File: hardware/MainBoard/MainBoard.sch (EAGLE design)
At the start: 220 parts, among them J1 CON-71741-2184-BOT, J2 CON-71741-2184-TOP, J3 CON-FTSH-105-01-L-DV-K, J4 CON-ZX62R-B-5P, J5 CON-SMA, J6 CON-SMA, J7 CON-RJ45-J0G-0007NL, J8 SWITCH-CJS-1200-1200, M1 MOUNT-HOLE3.3, M2 MOUNT-HOLE3.3, M3 MOUNT-HOLE3.3, M4 MOUNT-HOLE3.3, M5 FIDUCIAL1X2, M6 FIDUCIAL1X2, M7 FIDUCIAL1X2, M8 FIDUCIAL1X2, Q1 MMBT3904, SW1 SWITCH-KSC-201J, SW2 SWITCH-KSC-201J, U1 A2F500M3G-FG256, U2 MAX19706-T4877-4, U3 MAX19706-T4877-4, U4 USBLC6-2SC6, U5 FT232HL, U6 DP83848C-VBH48A, U7 93LC56BT-OT, U8 DS1818-10-SOT-23, U9 LMV112, X1 FOX924B, X2 ECX-31B, X3 ASEM1-C, X5 ECX-42-120

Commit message: Routed external clocks (still needs adjustment).
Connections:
- net D3V3: no longer C74.1, C75.1, C76.1
- net VJTAG: now also C74.1
- net VPUMP: now also C75.1, C76.1
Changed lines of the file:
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@@
 <part name="C74" library="MainBoard" deviceset="C" device="0402" value="0.1uF"/>
 <part name="U$87" library="MainBoard" deviceset="DGND" device=""/>
-<part name="U$88" library="MainBoard" deviceset="D3V3" device=""/>
 <part name="C75" library="MainBoard" deviceset="C" device="0402" value="0.33uF">
 <attribute name="VOTLAGE-RATING" value="16V"/>
@@
 </part>
 <part name="U$91" library="MainBoard" deviceset="DGND" device=""/>
-<part name="U$92" library="MainBoard" deviceset="D3V3" device=""/>
 <part name="PORT198" library="MainBoard" deviceset="PORT5" device=""/>
 <part name="PORT209" library="MainBoard" deviceset="PORT5" device=""/>
@@
 <part name="PORT359" library="MainBoard" deviceset="PORT7" device=""/>
 <part name="PORT360" library="MainBoard" deviceset="PORT7" device=""/>
+<part name="PORT361" library="MainBoard" deviceset="PORT5" device=""/>
+<part name="PORT362" library="MainBoard" deviceset="PORT5" device=""/>
 </parts>
 <sheets>
@@
 <rectangle x1="50.8" y1="81.28" x2="60.96" y2="83.82" layer="101"/>
 <text x="39.37" y="87.63" size="1.778" layer="101">Check if it should be negated</text>
-<rectangle x1="22.86" y1="68.58" x2="101.6" y2="91.44" layer="116"/>
 <rectangle x1="137.16" y1="121.92" x2="228.6" y2="165.1" layer="116"/>
 <rectangle x1="172.72" y1="43.18" x2="195.58" y2="78.74" layer="116"/>
 <rectangle x1="205.74" y1="43.18" x2="215.9" y2="78.74" layer="116"/>
 <rectangle x1="132.08" y1="81.28" x2="231.14" y2="119.38" layer="116"/>
+<rectangle x1="25.4" y1="71.12" x2="63.5" y2="91.44" layer="116"/>
+<rectangle x1="63.5" y1="71.12" x2="104.14" y2="81.28" layer="116"/>
 </plain>
 <instances>
@@
 <instance part="C74" gate="G$1" x="200.66" y="55.88"/>
 <instance part="U$87" gate="G$1" x="200.66" y="43.18"/>
-<instance part="U$88" gate="G$1" x="200.66" y="63.5"/>
 <instance part="C75" gate="G$1" x="218.44" y="55.88">
 <attribute name="VOTLAGE-RATING" x="218.44" y="55.88" size="1.778" layer="96" display="off"/>
@@
 </instance>
 <instance part="U$91" gate="G$1" x="220.98" y="43.18"/>
-<instance part="U$92" gate="G$1" x="220.98" y="63.5"/>
 <instance part="PORT198" gate="G$1" x="175.26" y="73.66" rot="R90"/>
 <instance part="PORT209" gate="G$1" x="182.88" y="73.66" rot="R90"/>
@@
 <instance part="PORT317" gate="G$1" x="193.04" y="45.72" rot="R270"/>
 <instance part="U$20" gate="G$1" x="30.48" y="33.02"/>
+<instance part="PORT361" gate="G$1" x="200.66" y="73.66" rot="R90"/>
+<instance part="PORT362" gate="G$1" x="220.98" y="73.66" rot="R90"/>
 </instances>
 <busses>
@@
 <wire x1="220.98" y1="114.3" x2="220.98" y2="116.84" width="0.1524" layer="91"/>
 <pinref part="U$90" gate="G$1" pin="D3V3"/>
-</segment>
-<segment>
-<pinref part="C74" gate="G$1" pin="1"/>
-<wire x1="200.66" y1="58.42" x2="200.66" y2="63.5" width="0.1524" layer="91"/>
-<pinref part="U$88" gate="G$1" pin="D3V3"/>
-</segment>
-<segment>
-<pinref part="C75" gate="G$1" pin="1"/>
-<wire x1="218.44" y1="58.42" x2="218.44" y2="60.96" width="0.1524" layer="91"/>
-<pinref part="C76" gate="G$1" pin="1"/>
-<wire x1="223.52" y1="58.42" x2="223.52" y2="60.96" width="0.1524" layer="91"/>
-<wire x1="223.52" y1="60.96" x2="220.98" y2="60.96" width="0.1524" layer="91"/>
-<pinref part="U$92" gate="G$1" pin="D3V3"/>
-<wire x1="220.98" y1="60.96" x2="218.44" y2="60.96" width="0.1524" layer="91"/>
-<wire x1="220.98" y1="63.5" x2="220.98" y2="60.96" width="0.1524" layer="91"/>
-<junction x="220.98" y="60.96"/>
 </segment>
 <segment>
@@
 <label x="144.78" y="106.68" size="1.778" layer="95" rot="MR0"/>
 </segment>
+<segment>
+<pinref part="C74" gate="G$1" pin="1"/>
+<wire x1="200.66" y1="58.42" x2="200.66" y2="63.5" width="0.1524" layer="91"/>
+<label x="200.66" y="66.04" size="1.778" layer="95" rot="R90"/>
+</segment>
 </net>
 <net name="VPUMP" class="0">
@@
 <label x="200.66" y="106.68" size="1.778" layer="95"/>
 </segment>
-</net>
+<segment>
+<pinref part="C75" gate="G$1" pin="1"/>
+<wire x1="218.44" y1="58.42" x2="218.44" y2="60.96" width="0.1524" layer="91"/>
+<pinref part="C76" gate="G$1" pin="1"/>
+<wire x1="223.52" y1="58.42" x2="223.52" y2="60.96" width="0.1524" layer="91"/>
+<wire x1="223.52" y1="60.96" x2="220.98" y2="60.96" width="0.1524" layer="91"/>
+<wire x1="220.98" y1="60.96" x2="218.44" y2="60.96" width="0.1524" layer="91"/>
+<wire x1="220.98" y1="63.5" x2="220.98" y2="60.96" width="0.1524" layer="91"/>
+<junction x="220.98" y="60.96"/>
+<label x="220.98" y="66.04" size="1.778" layer="95" rot="R90"/>
+</segment>
+</net>

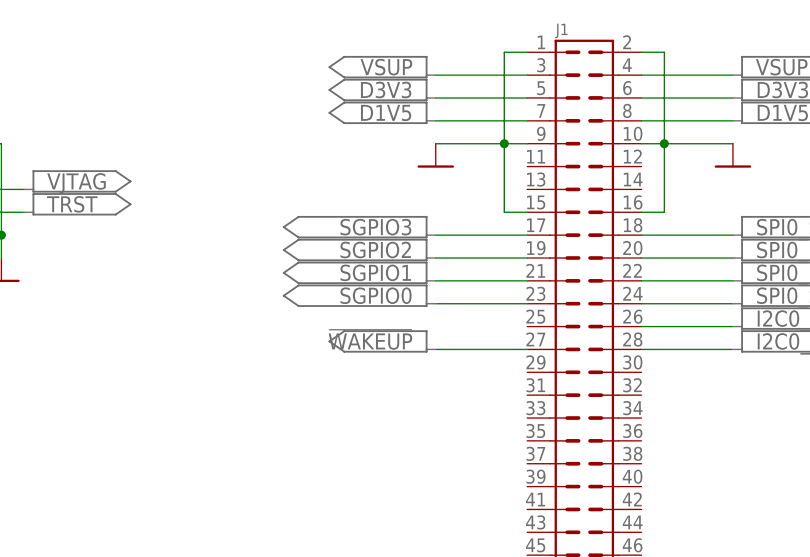
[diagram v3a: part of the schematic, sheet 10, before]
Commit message: 
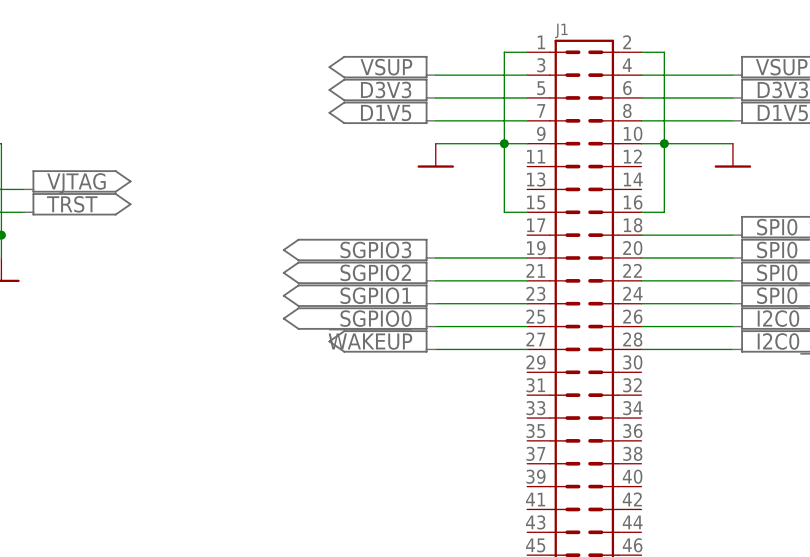
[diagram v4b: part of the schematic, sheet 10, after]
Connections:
- net NGPIO3: now also U1-EXTERNAL-MEMORY-CONTROLLER.EMC_CLK/GAA0/IO02NDB0V0; no longer U1-EXTERNAL-MEMORY-CONTROLLER.EMC_DB[6]/GEB0/IO79NDB5V0
- net NGPIO4: now also U1-IOB.IO84NDB5V0; no longer U1-EXTERNAL-MEMORY-CONTROLLER.EMC_DB[7]/GEB1/IO79PDB5V0
- net SGPIO0: now also J1.25; no longer J1.23
- net SGPIO1: now also J1.23; no longer J1.21
- net SGPIO2: now also J1.21, U1-EXTERNAL-MEMORY-CONTROLLER.EMC_DB[6]/GEB0/IO79NDB5V0; no longer J1.19, U1-EXTERNAL-MEMORY-CONTROLLER.EMC_CLK/GAA0/IO02NDB0V0
- net SGPIO3: now also J1.19, U1-EXTERNAL-MEMORY-CONTROLLER.EMC_DB[7]/GEB1/IO79PDB5V0; no longer J1.17, U1-IOB.IO84NDB5V0

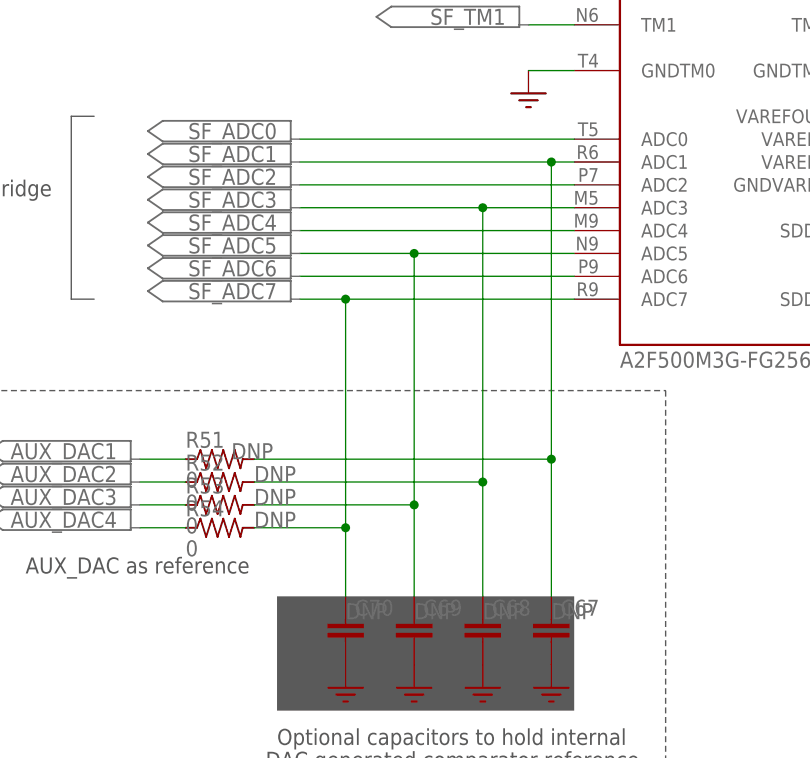
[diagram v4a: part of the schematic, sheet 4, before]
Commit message: 
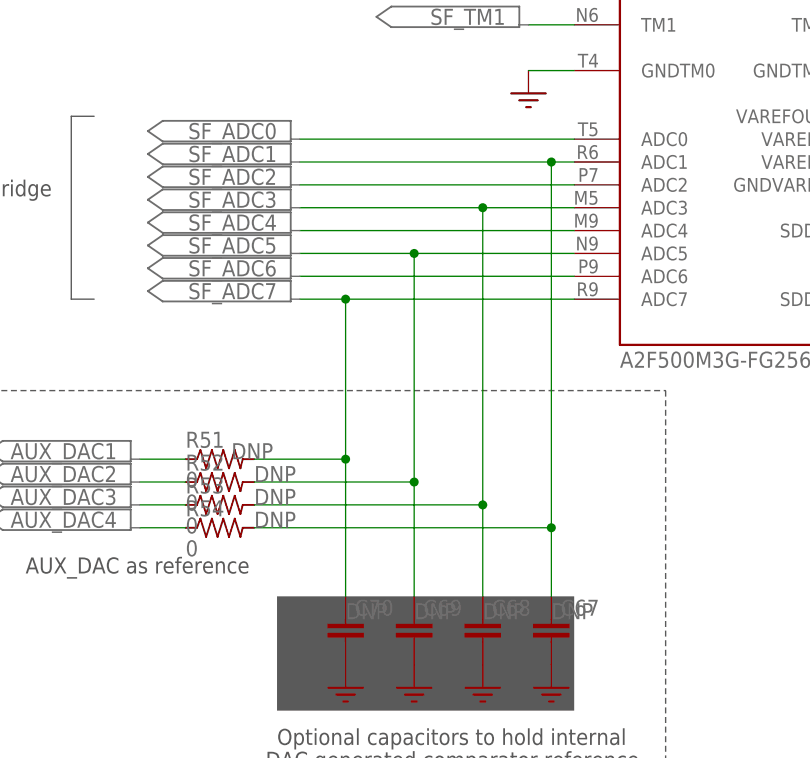
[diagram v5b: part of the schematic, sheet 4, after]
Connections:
- net NGPIO0: now also U1-EXTERNAL-MEMORY-CONTROLLER.EMC_DB[6]/GEB0/IO79NDB5V0; no longer U1-EXTERNAL-MEMORY-CONTROLLER.EMC_DB[2]/IO77NDB5V0
- net NGPIO1: now also U1-EXTERNAL-MEMORY-CONTROLLER.EMC_DB[10]/IO86NPB5V0; no longer U1-EXTERNAL-MEMORY-CONTROLLER.EMC_DB[5]/GEA1/IO78PPB5V0
- net NGPIO2: now also U1-EXTERNAL-MEMORY-CONTROLLER.EMC_DB[11]/IO86PPB5V0; no longer U1-EXTERNAL-MEMORY-CONTROLLER.EMC_DB[8]/GEC0/IO80NDB5V0
- net SF_ADC1: now also R54.2; no longer R51.2
- net SF_ADC3: now also R53.2; no longer R52.2
- net SF_ADC5: now also R52.2; no longer R53.2
- net SF_ADC7: now also R51.2; no longer R54.2
- net SGPIO0: now also U1-EXTERNAL-MEMORY-CONTROLLER.EMC_DB[5]/GEA1/IO78PPB5V0; no longer U1-EXTERNAL-MEMORY-CONTROLLER.EMC_DB[10]/IO86NPB5V0
- net SGPIO1: now also U1-EXTERNAL-MEMORY-CONTROLLER.EMC_DB[8]/GEC0/IO80NDB5V0; no longer U1-EXTERNAL-MEMORY-CONTROLLER.EMC_DB[11]/IO86PPB5V0
- net SGPIO2: now also U1-EXTERNAL-MEMORY-CONTROLLER.EMC_DB[2]/IO77NDB5V0; no longer U1-EXTERNAL-MEMORY-CONTROLLER.EMC_DB[6]/GEB0/IO79NDB5V0
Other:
- note added: "Check assignment order (routing!)"
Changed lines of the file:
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@@
 <text x="205.74" y="60.96" size="1.778" layer="97" rot="R90">VAREF0</text>
 <text x="213.36" y="60.96" size="1.778" layer="97" rot="R90">VAREF1</text>
+<rectangle x1="73.66" y1="53.34" x2="106.68" y2="63.5" layer="98"/>
+<text x="71.12" y="50.8" size="1.778" layer="98">Check assignment order (routing!)</text>
+<rectangle x1="40.64" y1="50.8" x2="71.12" y2="68.58" layer="116"/>
+<rectangle x1="71.12" y1="35.56" x2="111.76" y2="50.8" layer="116"/>
+<rectangle x1="132.08" y1="63.5" x2="154.94" y2="83.82" layer="116"/>
+<rectangle x1="182.88" y1="38.1" x2="226.06" y2="73.66" layer="116"/>
+<rectangle x1="142.24" y1="99.06" x2="185.42" y2="119.38" layer="116"/>
 </plain>
 <instances>
@@
 <wire x1="101.6" y1="96.52" x2="73.66" y2="96.52" width="0.1524" layer="91"/>
 <junction x="101.6" y="96.52"/>
-<wire x1="101.6" y1="48.26" x2="101.6" y2="63.5" width="0.1524" layer="91"/>
-<pinref part="R51" gate="G$1" pin="2"/>
-<wire x1="101.6" y1="63.5" x2="101.6" y2="96.52" width="0.1524" layer="91"/>
-<wire x1="68.58" y1="63.5" x2="101.6" y2="63.5" width="0.1524" layer="91"/>
-<junction x="101.6" y="63.5"/>
+<wire x1="101.6" y1="48.26" x2="101.6" y2="55.88" width="0.1524" layer="91"/>
+<pinref part="R54" gate="G$1" pin="2"/>
+<wire x1="101.6" y1="55.88" x2="101.6" y2="96.52" width="0.1524" layer="91"/>
+<wire x1="68.58" y1="55.88" x2="101.6" y2="55.88" width="0.1524" layer="91"/>
+<junction x="101.6" y="55.88"/>
 </segment>
 </net>
@@
 <wire x1="93.98" y1="91.44" x2="73.66" y2="91.44" width="0.1524" layer="91"/>
 <junction x="93.98" y="91.44"/>
-<wire x1="93.98" y1="48.26" x2="93.98" y2="60.96" width="0.1524" layer="91"/>
-<pinref part="R52" gate="G$1" pin="2"/>
-<wire x1="93.98" y1="60.96" x2="93.98" y2="91.44" width="0.1524" layer="91"/>
-<wire x1="68.58" y1="60.96" x2="93.98" y2="60.96" width="0.1524" layer="91"/>
-<junction x="93.98" y="60.96"/>
+<wire x1="93.98" y1="48.26" x2="93.98" y2="58.42" width="0.1524" layer="91"/>
+<pinref part="R53" gate="G$1" pin="2"/>
+<wire x1="93.98" y1="58.42" x2="93.98" y2="91.44" width="0.1524" layer="91"/>
+<wire x1="68.58" y1="58.42" x2="93.98" y2="58.42" width="0.1524" layer="91"/>
+<junction x="93.98" y="58.42"/>
 </segment>
 </net>
@@
 <wire x1="86.36" y1="86.36" x2="73.66" y2="86.36" width="0.1524" layer="91"/>
 <junction x="86.36" y="86.36"/>
-<wire x1="86.36" y1="48.26" x2="86.36" y2="58.42" width="0.1524" layer="91"/>
-<pinref part="R53" gate="G$1" pin="2"/>
-<wire x1="86.36" y1="58.42" x2="86.36" y2="86.36" width="0.1524" layer="91"/>
-<wire x1="68.58" y1="58.42" x2="86.36" y2="58.42" width="0.1524" layer="91"/>
-<junction x="86.36" y="58.42"/>
+<wire x1="86.36" y1="48.26" x2="86.36" y2="60.96" width="0.1524" layer="91"/>
+<pinref part="R52" gate="G$1" pin="2"/>
+<wire x1="86.36" y1="60.96" x2="86.36" y2="86.36" width="0.1524" layer="91"/>
+<wire x1="68.58" y1="60.96" x2="86.36" y2="60.96" width="0.1524" layer="91"/>
+<junction x="86.36" y="60.96"/>
 </segment>
 </net>
@@
 <wire x1="78.74" y1="81.28" x2="73.66" y2="81.28" width="0.1524" layer="91"/>
 <junction x="78.74" y="81.28"/>
-<wire x1="78.74" y1="48.26" x2="78.74" y2="55.88" width="0.1524" layer="91"/>
-<pinref part="R54" gate="G$1" pin="2"/>
-<wire x1="78.74" y1="55.88" x2="78.74" y2="81.28" width="0.1524" layer="91"/>
-<wire x1="68.58" y1="55.88" x2="78.74" y2="55.88" width="0.1524" layer="91"/>
-<junction x="78.74" y="55.88"/>
+<wire x1="78.74" y1="48.26" x2="78.74" y2="63.5" width="0.1524" layer="91"/>
+<pinref part="R51" gate="G$1" pin="2"/>
+<wire x1="78.74" y1="63.5" x2="78.74" y2="81.28" width="0.1524" layer="91"/>
+<wire x1="68.58" y1="63.5" x2="78.74" y2="63.5" width="0.1524" layer="91"/>
+<junction x="78.74" y="63.5"/>
 </segment>
 </net>
@@
 </segment>
 </net>
-<net name="NGPIO0" class="0">
-<segment>
-<pinref part="U1" gate="-EXTERNAL-MEMORY-CONTROLLER" pin="EMC_DB[2]/IO77NDB5V0"/>
-<wire x1="215.9" y1="149.86" x2="220.98" y2="149.86" width="0.1524" layer="91"/>
-<label x="223.52" y="149.86" size="1.778" layer="95"/>
-</segment>
-</net>
 <net name="NGPIO1" class="0">
 <segment>
-<pinref part="U1" gate="-EXTERNAL-MEMORY-CONTROLLER" pin="EMC_DB[5]/GEA1/IO78PPB5V0"/>
-<wire x1="215.9" y1="142.24" x2="220.98" y2="142.24" width="0.1524" layer="91"/>
-<label x="223.52" y="142.24" size="1.778" layer="95"/>
-</segment>
-</net>
-<net name="SGPIO0" class="0">
-<segment>
 <pinref part="U1" gate="-EXTERNAL-MEMORY-CONTROLLER" pin="EMC_DB[10]/IO86NPB5V0"/>
 <wire x1="215.9" y1="129.54" x2="220.98" y2="129.54" width="0.1524" layer="91"/>
@@
 </segment>
 </net>
-<net name="SGPIO1" class="0">
+<net name="NGPIO2" class="0">
 <segment>
 <pinref part="U1" gate="-EXTERNAL-MEMORY-CONTROLLER" pin="EMC_DB[11]/IO86PPB5V0"/>
@@
 </segment>
 </net>
-<net name="NGPIO2" class="0">
-<segment>
-<pinref part="U1" gate="-EXTERNAL-MEMORY-CONTROLLER" pin="EMC_DB[8]/GEC0/IO80NDB5V0"/>
-<wire x1="215.9" y1="134.62" x2="220.98" y2="134.62" width="0.1524" layer="91"/>
-<label x="223.52" y="134.62" size="1.778" layer="95"/>
-</segment>
-</net>
 <net name="SGPIO3" class="0">
 <segment>
@@
 <net name="SGPIO2" class="0">
 <segment>
-<pinref part="U1" gate="-EXTERNAL-MEMORY-CONTROLLER" pin="EMC_DB[6]/GEB0/IO79NDB5V0"/>
-<wire x1="215.9" y1="139.7" x2="220.98" y2="139.7" width="0.1524" layer="91"/>
-<label x="223.52" y="139.7" size="1.778" layer="95"/>
+<pinref part="U1" gate="-EXTERNAL-MEMORY-CONTROLLER" pin="EMC_DB[2]/IO77NDB5V0"/>
+<wire x1="215.9" y1="149.86" x2="220.98" y2="149.86" width="0.1524" layer="91"/>
+<label x="223.52" y="149.86" size="1.778" layer="95"/>
 </segment>
 </net>
@@
 </segment>
 </net>
+<net name="SGPIO1" class="0">
+<segment>
+<pinref part="U1" gate="-EXTERNAL-MEMORY-CONTROLLER" pin="EMC_DB[8]/GEC0/IO80NDB5V0"/>
+<wire x1="215.9" y1="134.62" x2="220.98" y2="134.62" width="0.1524" layer="91"/>
+<label x="223.52" y="134.62" size="1.778" layer="95"/>
+</segment>
+</net>
+<net name="SGPIO0" class="0">
+<segment>
+<pinref part="U1" gate="-EXTERNAL-MEMORY-CONTROLLER" pin="EMC_DB[5]/GEA1/IO78PPB5V0"/>
+<wire x1="215.9" y1="142.24" x2="220.98" y2="142.24" width="0.1524" layer="91"/>
+<label x="223.52" y="142.24" size="1.778" layer="95"/>
+</segment>
+</net>
+<net name="NGPIO0" class="0">
+<segment>
+<pinref part="U1" gate="-EXTERNAL-MEMORY-CONTROLLER" pin="EMC_DB[6]/GEB0/IO79NDB5V0"/>
+<wire x1="215.9" y1="139.7" x2="220.98" y2="139.7" width="0.1524" layer="91"/>
+<label x="223.52" y="139.7" size="1.778" layer="95"/>
+</segment>
+</net>
